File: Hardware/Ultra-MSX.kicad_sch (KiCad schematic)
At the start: 9 parts

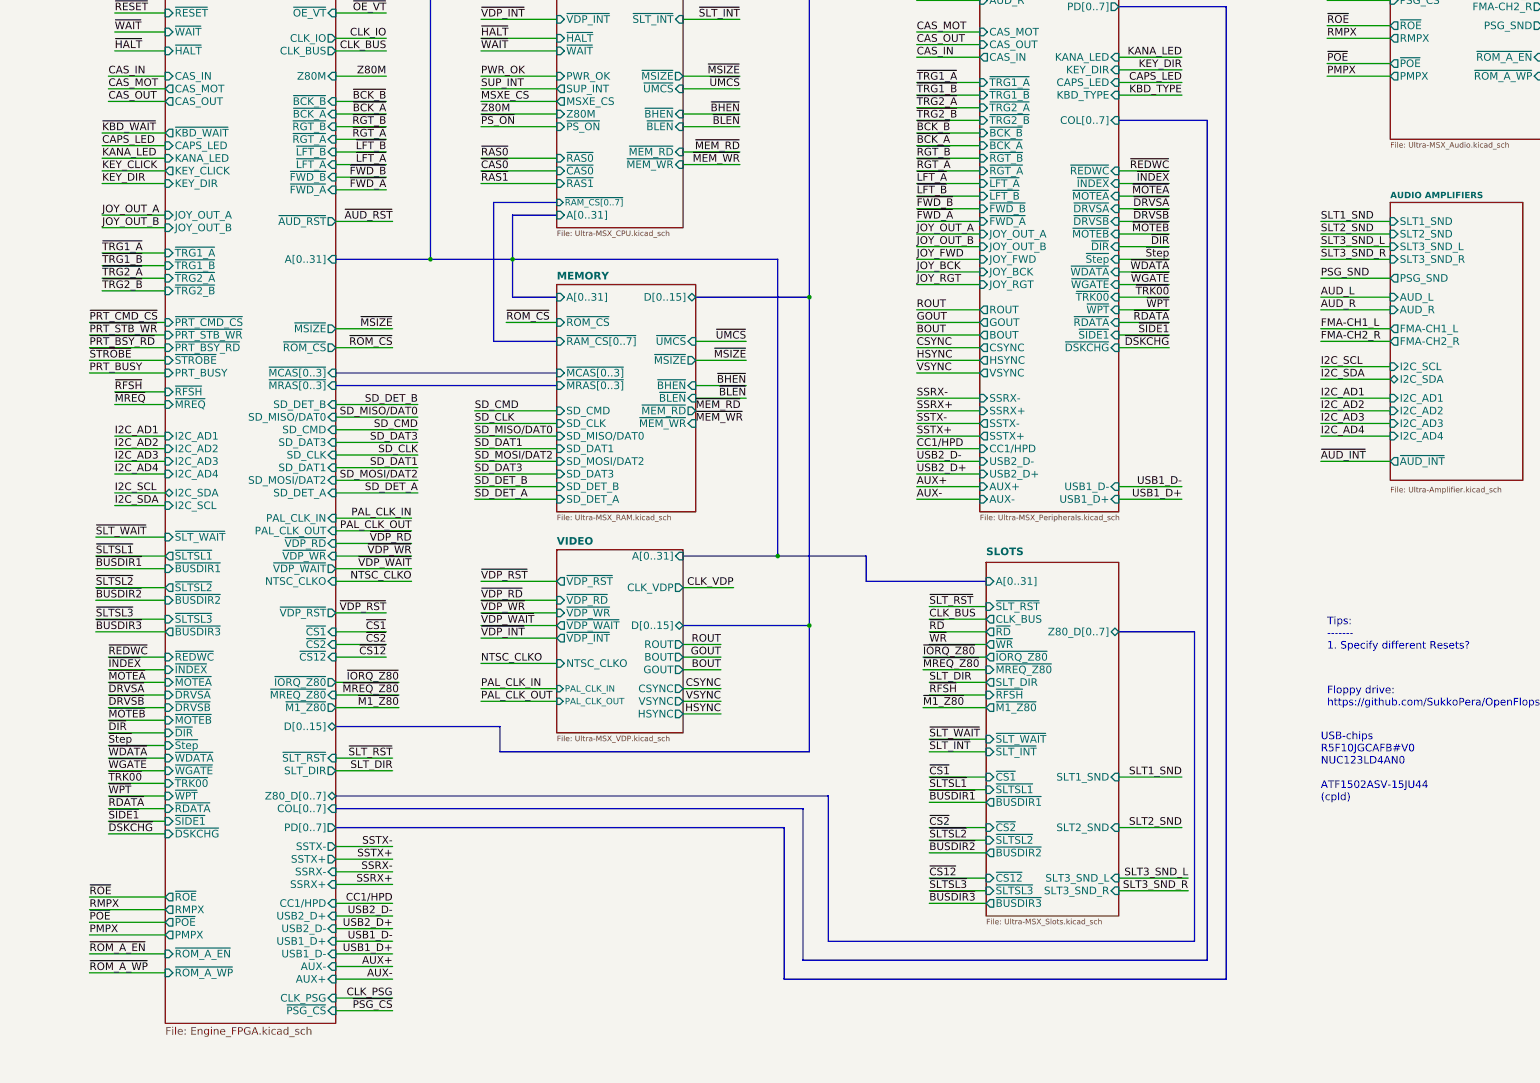
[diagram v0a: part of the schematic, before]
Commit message: Multiple redesigns of the IO-shield. Replaced FPGA with lower pin-count AT10K, since the higher pin-count one is now obsolete.
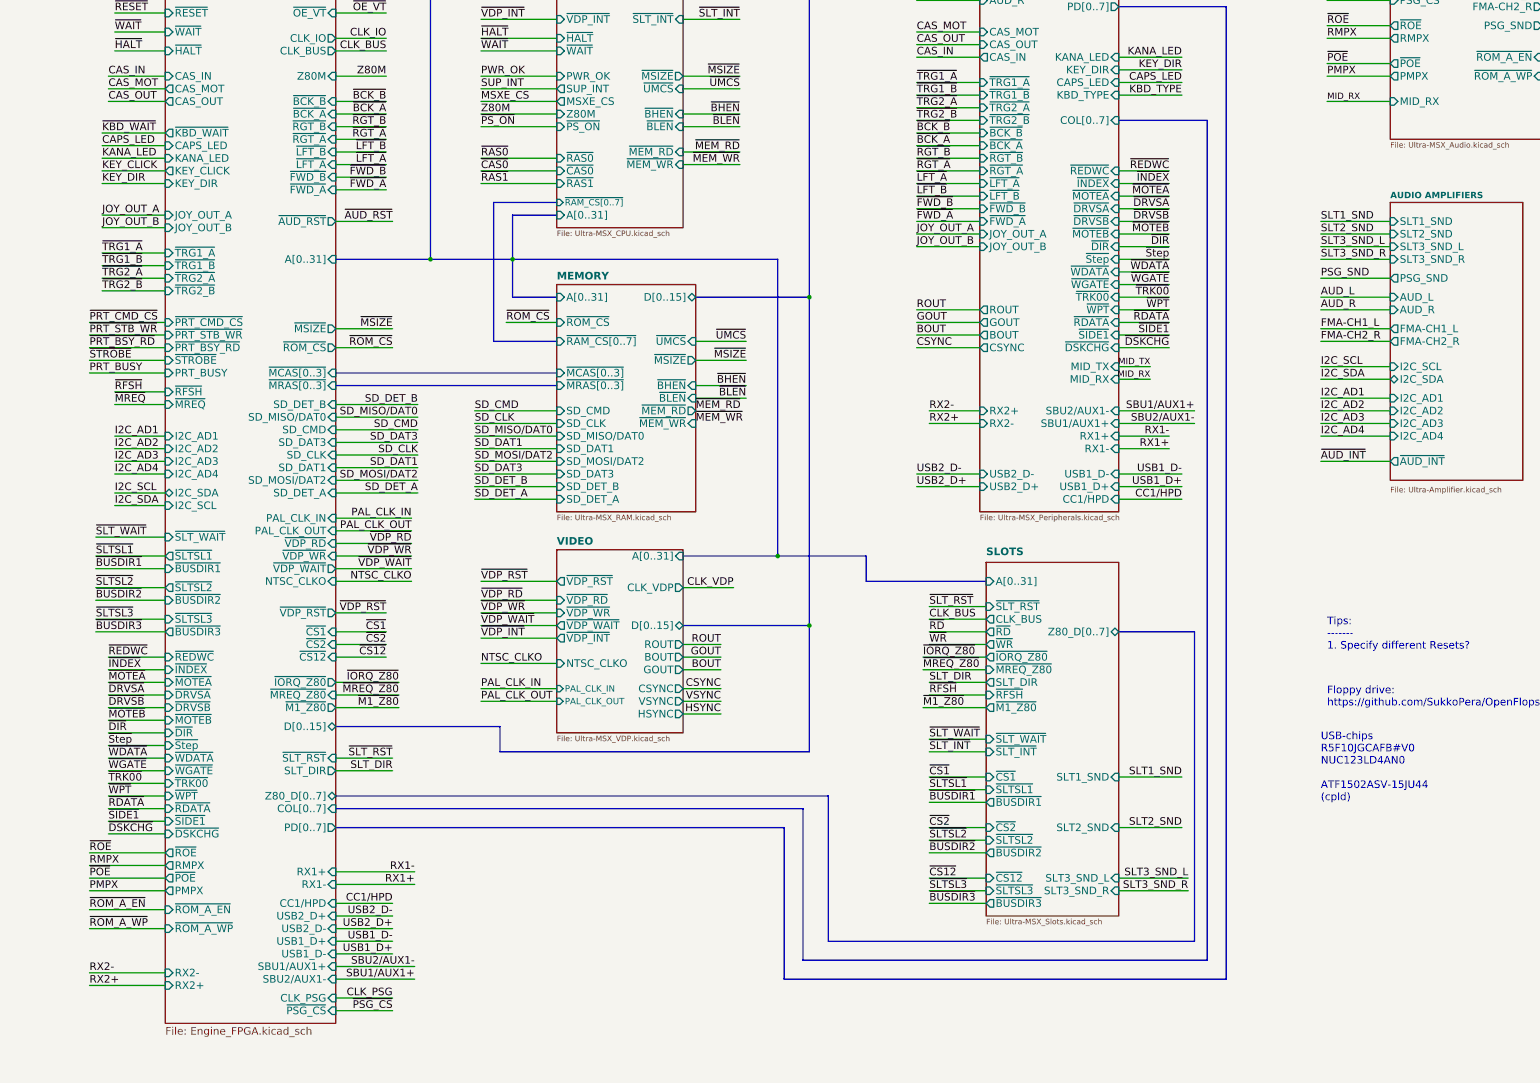
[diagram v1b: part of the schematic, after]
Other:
- sheet AUDIO ports: added MID_RX; removed none
- sheet MSX ENGINE ports: added RX1+, RX1-, RX2+, RX2-, SBU1/AUX1+, SBU2/AUX1-; removed AUX+, AUX-, SSRX+, SSRX-, SSTX+, SSTX-
- sheet PERIPHERALS ports: added MID_RX, MID_TX, RX1+, RX1-, RX2+, RX2-, SBU1/AUX1+, SBU2/AUX1-; removed AUX+, AUX-, HSYNC, JOY_BCK, JOY_FWD, JOY_RGT, SSRX+, SSRX-, SSTX+, SSTX-, VSYNC

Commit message: Added cooler and CPU-mount footprints, as well as Indication LEDs.
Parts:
- removed HS1: Aavid_Heatsink_2Pin, LRJ:Heatsink_35x35mm_SpringFixation, symbol LRJ-parts:Aavid_Heatsink_2Pin
- added HS2: Heatsink_Scythe_Fuma2, LRJ:Heatsink_Scythe_FUMA_129x137mm, symbol LRJ-parts:Heatsink_Scythe_Fuma2
- added J7, J8: AM4_bracket, LRJ:AM4_Cooler-bracket, symbol LRJ-parts:AM4_bracket
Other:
- sheet MEMORY ports: added I2C_SCL, I2C_SDA, MCKE0, MCKE1; removed none
- sheet MSX ENGINE ports: added CLK_VDP, MCKE0, MCKE1, SWDCLK/RX1-, SWDIO/RX1+, SWO/RX2-, nRESET/RX2+; removed RX1+, RX1-, RX2+, RX2-, SBU1/AUX1+, SBU2/AUX1-
- sheet PERIPHERALS ports: added GND/SBU2, SWDCLK/RX1-, SWDIO/RX1+, SWO/RX2-, VCT/SBU1, nRESET/RX2+; removed RX1+, RX1-, RX2+, RX2-, SBU1/AUX1+, SBU2/AUX1-
- sheet POWER ports: added GND/SBU2, VCT/SBU1; removed none
- sheet PROCESSOR ports: added none; removed CLK_VDP
- note added: "CPU socket"
- moved on the sheet: Cart1, Cart2, Cart3, Case1, H1, H2, H3, H4

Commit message: Started fixing many small issues.
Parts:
- HS2: now left out of the parts list
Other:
- sheet MSX ENGINE renamed MSX ENGINE (chipset)
- sheet AUDIO ports: added WAVE_L, WAVE_R, ~{ROM_A_OE}, ~{ROM_A_WE}, ~{RY_BY}; removed none
- sheet AUDIO AMPLIFIERS ports: added I2C_AD[1..5], KEY_CLICK, WAVE_L, WAVE_R; removed I2C_AD1, I2C_AD2, I2C_AD3, I2C_AD4
- sheet MEMORY ports: added DQMB[0..7], MCLK0, MCLK1, MD[0..63], ~{CAS0}, ~{RAS0}; removed ~{BHEN}, ~{BLEN}, ~{MCAS[0..3]}, ~{MRAS[0..3]}
- sheet MSX ENGINE (chipset) ports: added DQMB[0..7], FanCtrl[1..3], FanSen[1..3], HDD_PWM, I2C_AD[1..5], MD[0..63], MID_RX, MID_TX, VID_ID, ~{BHEN}, ~{BLEN}, ~{ROM_A_OE}, ~{ROM_A_WE}, ~{RY_BY}, ~{SLT_CS12}, ~{SLT_CS1}, ~{SLT_CS2}; removed I2C_AD1, I2C_AD2, I2C_AD3, I2C_AD4, ~{CS12}, ~{CS1}, ~{CS2}, ~{MCAS[0..3]}, ~{MRAS[0..3]}, ~{MREQ}, ~{PRT_BSY_RD}, ~{PRT_CMD_CS}, ~{PRT_STB_WR}
- sheet PERIPHERALS ports: added BLANK, FanCtrl[1..3], FanSen[1..3]; removed GND/SBU2, VCT/SBU1
- sheet POWER ports: added PLED+; removed GND/SBU2, VCT/SBU1
- sheet PROCESSOR ports: added HDD_PWM, PLED+; removed none
- sheet SLOTS ports: added ~{SLT_CS12}, ~{SLT_CS1}, ~{SLT_CS2}; removed ~{CS12}, ~{CS1}, ~{CS2}
- sheet VIDEO ports: added BLANK, VID_ID; removed none
- note added: "Computer-case"
- note removed: "Floppy drive: https://github.com/SukkoPera/OpenFlops"
- note removed: "Tips: ------- 1. Specify different Resets?"
- note removed: "USB-chips R5F10JGCAFB#V0 NUC123LD4AN0 ATF1502ASV-15JU44 (cpld)"

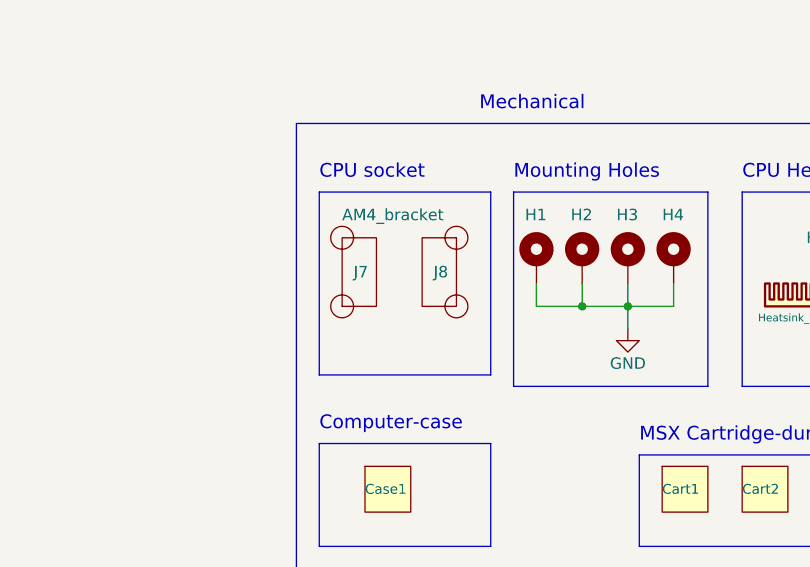
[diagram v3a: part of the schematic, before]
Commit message: Updated the readme, silenced multiple errors in Kicad regarding simulation-files.
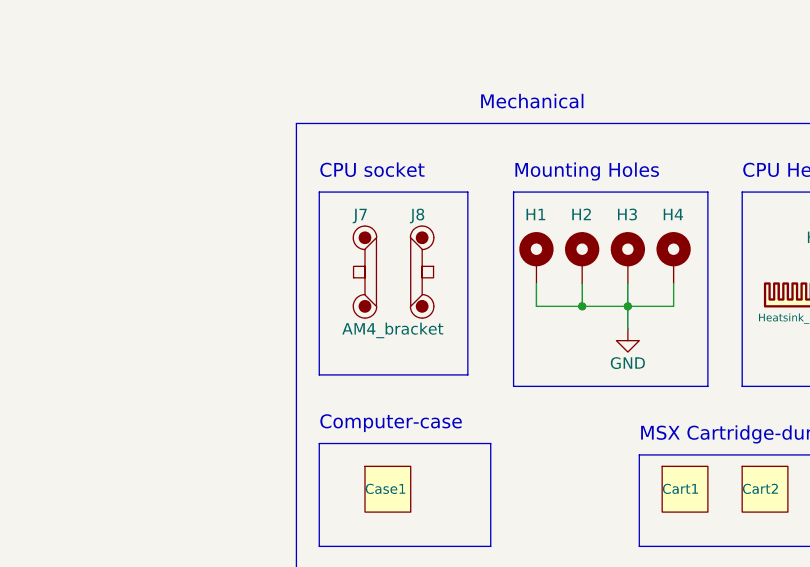
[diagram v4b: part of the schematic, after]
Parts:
- Cart1, Cart2, Cart3, Case1, H1, H2, H3, H4: now left out of the parts list
- J7, J8: MPN (none) -> n/a; Manufacturer (none) -> n/a
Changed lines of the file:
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@@
     (stroke (width 0) (type default))
   )
-  (polyline (pts (xy 356.87 233.68) (xy 356.87 213.36))
+  (polyline (pts (xy 354.33 233.68) (xy 354.33 213.36))
     (stroke (width 0) (type default))
   )
@@
     (stroke (width 0) (type default))
   )
-  (polyline (pts (xy 337.82 213.36) (xy 356.87 213.36))
+  (polyline (pts (xy 337.82 213.36) (xy 354.33 213.36))
     (stroke (width 0) (type default))
   )
@@
     (stroke (width 0) (type default))
   )
-  (polyline (pts (xy 337.82 233.68) (xy 356.87 233.68))
+  (polyline (pts (xy 337.82 233.68) (xy 354.33 233.68))
     (stroke (width 0) (type default))
   )
@@
   )
   (symbol (lib_id "Ultra-MSX:MSX-cartridge_dummy") (at 387.35 246.38 0) (unit 1)
-    (in_bom yes) (on_board yes) (dnp no)
+    (in_bom no) (on_board yes) (dnp no)
     (property "Reference" "Cart2" (at 384.81 246.38 0)
       (effects (font (size 1.0922 1.0922)) (justify left))
@@
     )
     (property "Manufacturer" "n/a" (at 393.7 243.84 0)
+      (effects (font (size 1.27 1.27)) hide)
+    )
+    (property "Sim.Enable" "0" (at 387.35 246.38 0)
       (effects (font (size 1.27 1.27)) hide)
     )
@@
   )
   (symbol (lib_id "Ultra-MSX:MSX-cartridge_dummy") (at 396.24 246.38 0) (unit 1)
-    (in_bom yes) (on_board yes) (dnp no)
+    (in_bom no) (on_board yes) (dnp no)
     (property "Reference" "Cart3" (at 393.7 246.38 0)
       (effects (font (size 1.0922 1.0922)) (justify left))
@@
     )
     (property "Manufacturer" "n/a" (at 402.59 243.84 0)
+      (effects (font (size 1.27 1.27)) hide)
+    )
+    (property "Sim.Enable" "0" (at 396.24 246.38 0)
       (effects (font (size 1.27 1.27)) hide)
     )
@@
   )
   (symbol (lib_id "Ultra-MSX:MSX-cartridge_dummy") (at 378.46 246.38 0) (unit 1)
-    (in_bom yes) (on_board yes) (dnp no)
+    (in_bom no) (on_board yes) (dnp no)
     (property "Reference" "Cart1" (at 375.92 246.38 0)
       (effects (font (size 1.0922 1.0922)) (justify left))
@@
     )
     (property "Manufacturer" "n/a" (at 384.81 243.84 0)
+      (effects (font (size 1.27 1.27)) hide)
+    )
+    (property "Sim.Enable" "0" (at 378.46 246.38 0)
       (effects (font (size 1.27 1.27)) hide)
     )
@@
   )
   (symbol (lib_id "Mechanical:MountingHole_Pad") (at 361.95 220.98 0) (unit 1)
-    (in_bom yes) (on_board yes) (dnp no)
+    (in_bom no) (on_board yes) (dnp no)
     (property "Reference" "H1" (at 360.68 215.9 0)
       (effects (font (size 1.27 1.27)) (justify left))
@@
     )
     (property "Datasheet" "~" (at 361.95 220.98 0)
+      (effects (font (size 1.27 1.27)) hide)
+    )
+    (property "Sim.Enable" "0" (at 361.95 220.98 0)
       (effects (font (size 1.27 1.27)) hide)
     )
@@
   )
   (symbol (lib_id "Mechanical:MountingHole_Pad") (at 367.03 220.98 0) (unit 1)
-    (in_bom yes) (on_board yes) (dnp no)
+    (in_bom no) (on_board yes) (dnp no)
     (property "Reference" "H2" (at 365.76 215.9 0)
       (effects (font (size 1.27 1.27)) (justify left))
@@
     )
     (property "Datasheet" "~" (at 367.03 220.98 0)
+      (effects (font (size 1.27 1.27)) hide)
+    )
+    (property "Sim.Enable" "0" (at 367.03 220.98 0)
       (effects (font (size 1.27 1.27)) hide)
     )
@@
   )
   (symbol (lib_id "Mechanical:MountingHole_Pad") (at 372.11 220.98 0) (unit 1)
-    (in_bom yes) (on_board yes) (dnp no)
+    (in_bom no) (on_board yes) (dnp no)
     (property "Reference" "H3" (at 370.84 215.9 0)
       (effects (font (size 1.27 1.27)) (justify left))
@@
     )
     (property "Datasheet" "~" (at 372.11 220.98 0)
+      (effects (font (size 1.27 1.27)) hide)
+    )
+    (property "Sim.Enable" "0" (at 372.11 220.98 0)
       (effects (font (size 1.27 1.27)) hide)
     )
@@
   )
   (symbol (lib_id "Mechanical:MountingHole_Pad") (at 377.19 220.98 0) (unit 1)
-    (in_bom yes) (on_board yes) (dnp no)
+    (in_bom no) (on_board yes) (dnp no)
     (property "Reference" "H4" (at 375.92 215.9 0)
       (effects (font (size 1.27 1.27)) (justify left))
@@
     )
     (property "Datasheet" "~" (at 377.19 220.98 0)
+      (effects (font (size 1.27 1.27)) hide)
+    )
+    (property "Sim.Enable" "0" (at 377.19 220.98 0)
       (effects (font (size 1.27 1.27)) hide)
     )
@@
   )
   (symbol (lib_id "Ultra-MSX:MSX-DANv4-case_dummy") (at 345.44 246.38 0) (unit 1)
-    (in_bom yes) (on_board yes) (dnp no)
+    (in_bom no) (on_board yes) (dnp no)
     (property "Reference" "Case1" (at 342.9 246.38 0)
       (effects (font (size 1.0922 1.0922)) (justify left))
@@
     )
     (property "Manufacturer" "DAN Cases" (at 358.14 243.84 0)
+      (effects (font (size 1.27 1.27)) hide)
+    )
+    (property "Sim.Enable" "0" (at 345.44 246.38 0)
       (effects (font (size 1.27 1.27)) hide)
     )
@@
     )
   )
-  (symbol (lib_id "LRJ-parts:AM4_bracket") (at 351.79 222.25 270) (unit 1)
+  (symbol (lib_id "LRJ-parts:AM4_bracket") (at 349.25 222.25 270) (unit 1)
     (in_bom yes) (on_board yes) (dnp no)
-    (property "Reference" "J8" (at 350.52 222.25 90)
+    (property "Reference" "J8" (at 347.98 215.9 90)
       (effects (font (size 1.27 1.27)) (justify left))
     )
-    (property "Value" "AM4_bracket" (at 340.36 215.9 90)
+    (property "Value" "AM4_bracket" (at 340.36 228.6 90)
       (effects (font (size 1.27 1.27)) (justify left))
     )
-    (property "Footprint" "LRJ:AM4_Cooler-bracket" (at 344.17 222.25 0)
-      (effects (font (size 1.27 1.27)) hide)
-    )
-    (property "Datasheet" "" (at 350.52 222.25 0)
+    (property "Footprint" "LRJ:AM4_Cooler-bracket" (at 341.63 222.25 0)
+      (effects (font (size 1.27 1.27)) hide)
+    )
+    (property "Datasheet" "" (at 347.98 222.25 0)
+      (effects (font (size 1.27 1.27)) hide)
+    )
+    (property "Sim.Enable" "0" (at 347.98 222.25 0)
+      (effects (font (size 1.27 1.27)) hide)
+    )
+    (property "MPN" "n/a" (at 350.52 232.41 0)
+      (effects (font (size 1.27 1.27)) hide)
+    )
+    (property "Manufacturer" "n/a" (at 352.425 232.41 0)
       (effects (font (size 1.27 1.27)) hide)
     )
@@
     )
   )
-  (symbol (lib_id "LRJ-parts:AM4_bracket") (at 341.63 222.25 90) (unit 1)
+  (symbol (lib_id "LRJ-parts:AM4_bracket") (at 342.9 222.25 90) (unit 1)
     (in_bom yes) (on_board yes) (dnp no)
-    (property "Reference" "J7" (at 341.63 222.25 90)
+    (property "Reference" "J7" (at 341.63 215.9 90)
       (effects (font (size 1.27 1.27)) (justify right))
     )
-    (property "Value" "AM4_bracket" (at 340.36 228.6 90)
+    (property "Value" "AM4_bracket" (at 341.63 228.6 90)
       (effects (font (size 1.27 1.27)) (justify right) hide)
     )
-    (property "Footprint" "LRJ:AM4_Cooler-bracket" (at 349.25 222.25 0)
-      (effects (font (size 1.27 1.27)) hide)
-    )
-    (property "Datasheet" "" (at 342.9 222.25 0)
+    (property "Footprint" "LRJ:AM4_Cooler-bracket" (at 350.52 222.25 0)
+      (effects (font (size 1.27 1.27)) hide)
+    )
+    (property "Datasheet" "" (at 344.17 222.25 0)
+      (effects (font (size 1.27 1.27)) hide)
+    )
+    (property "Sim.Enable" "0" (at 344.17 222.25 0)
+      (effects (font (size 1.27 1.27)) hide)
+    )
+    (property "MPN" "n/a" (at 341.63 212.09 0)
+      (effects (font (size 1.27 1.27)) hide)
+    )
+    (property "Manufacturer" "n/a" (at 339.725 212.09 0)
       (effects (font (size 1.27 1.27)) hide)
     )
@@
       (effects (font (size 1.27 1.27)) hide)
     )
+    (property "Sim.Enable" "0" (at 394.97 226.06 0)
+      (effects (font (size 1.27 1.27)) hide)
+    )

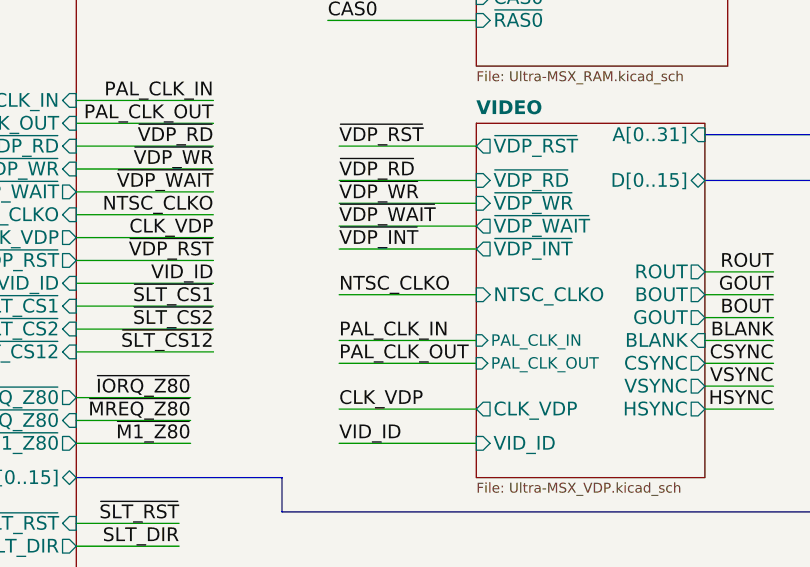
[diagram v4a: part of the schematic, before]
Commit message: Many tweaks and changes, such as a slight redesign of the VDP-baord.
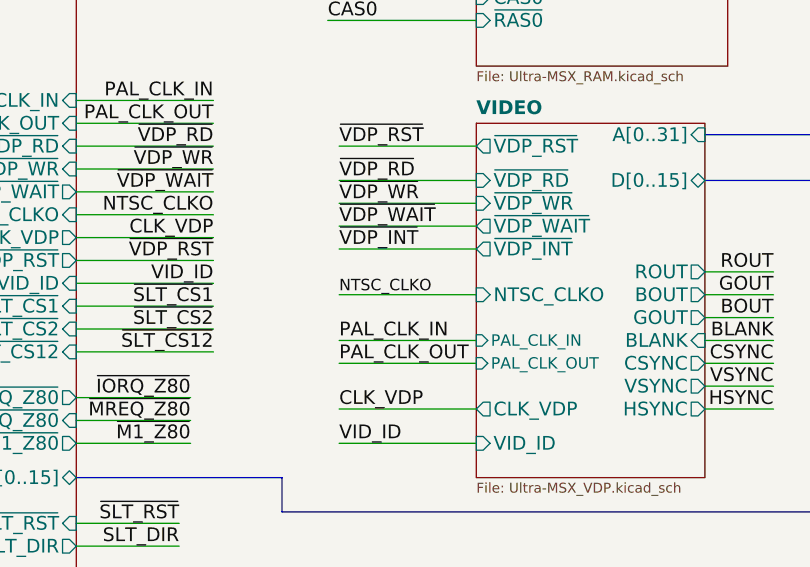
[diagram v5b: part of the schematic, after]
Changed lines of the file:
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@@
     (effects (font (size 1.524 1.524)) (justify right bottom))
+  )
+  (label "NTSC_CLKO" (at 130.81 179.07 0) (fields_autoplaced)
+    (effects (font (size 1.27 1.27)) (justify left bottom))
   )
   (label "MCKE1" (at 113.03 101.6 180) (fields_autoplaced)
@@
     (effects (font (size 1.524 1.524)) (justify left bottom))
   )
-  (label "NTSC_CLKO" (at 130.81 179.07 0) (fields_autoplaced)
-    (effects (font (size 1.524 1.524)) (justify left bottom))
-  )
